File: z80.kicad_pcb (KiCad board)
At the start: 2 copper layers, 104.1 x 121.9 mm, 53 parts, among them P1 CONN_02X20, SW1 RESET, SW2 STEP, U1 Z80CPU, U2 74HC04, U3 74LS138, U4 LM555N, U5 74HC74, U6 LM555N, Y1 7.3728MHz

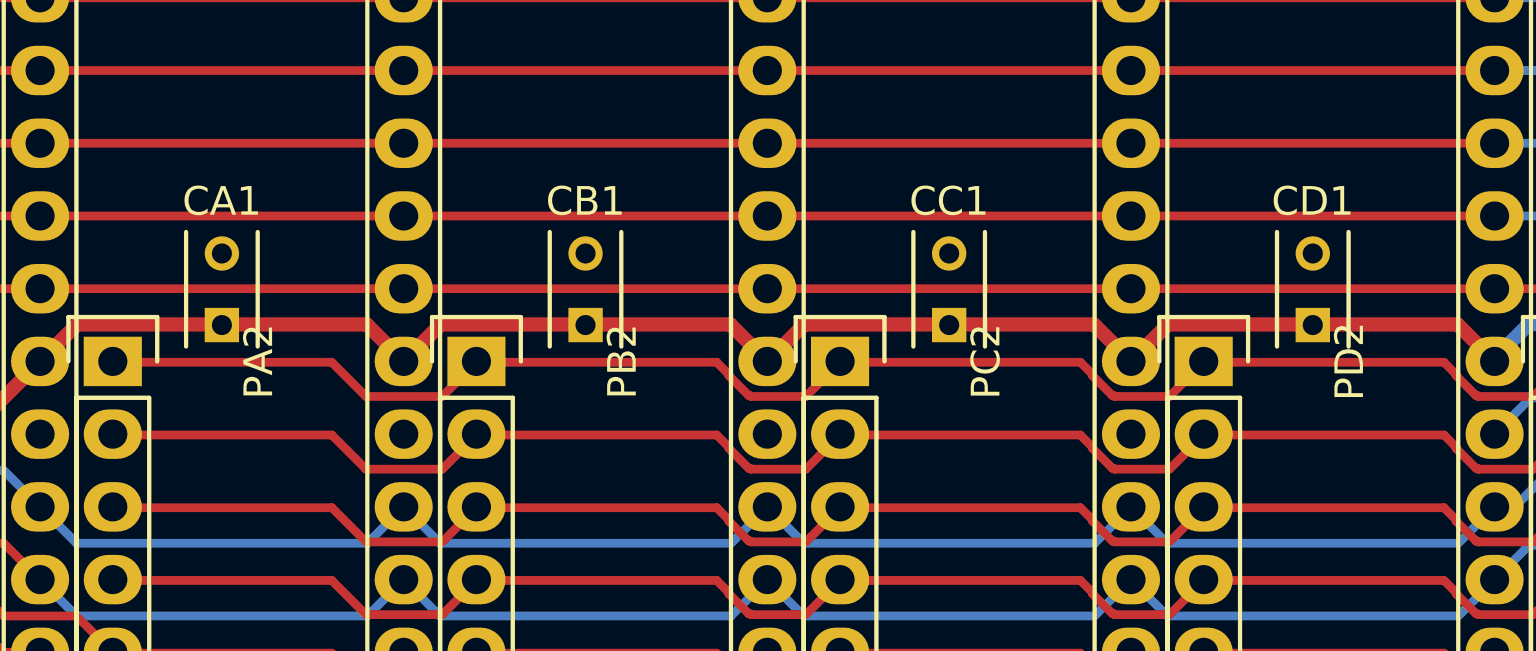
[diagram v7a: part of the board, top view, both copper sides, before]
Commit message: Flipped the decoupling caps around for neatness
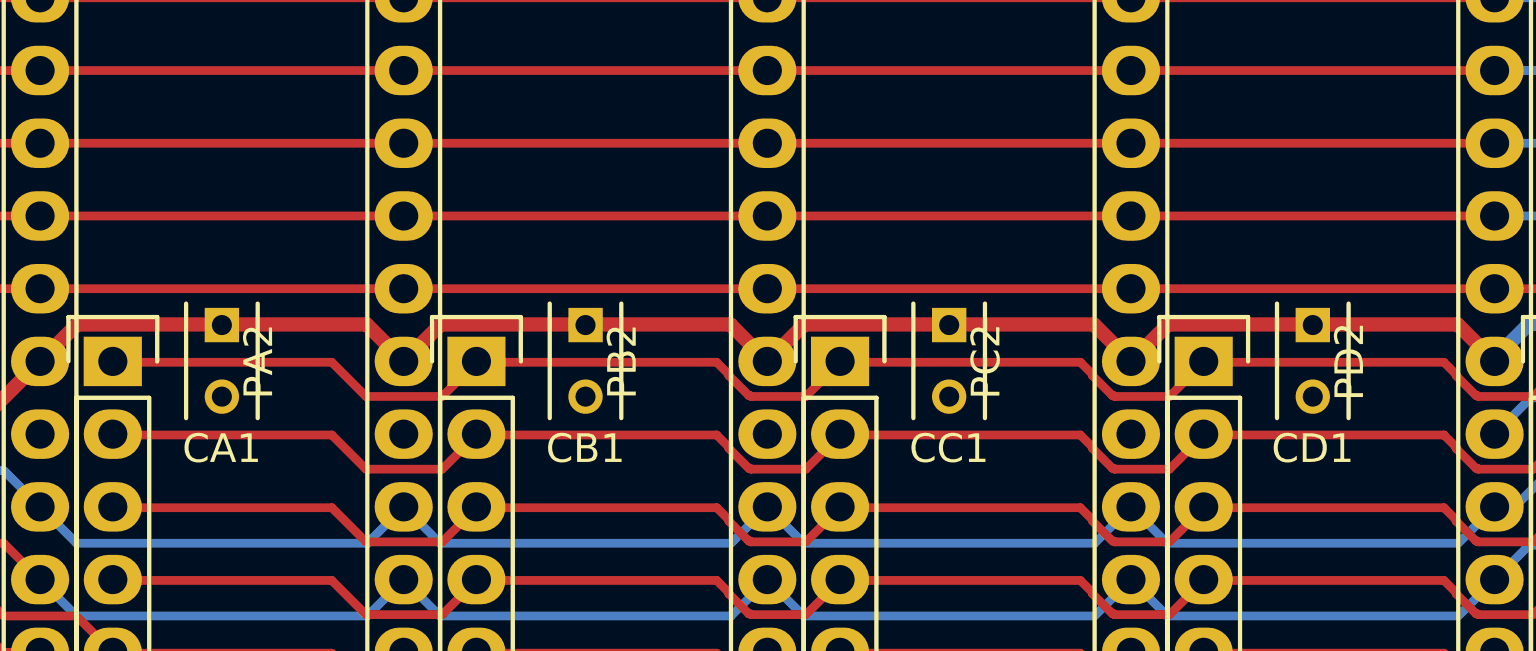
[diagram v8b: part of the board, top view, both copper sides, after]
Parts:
- turned CA1 to 270 degrees
- turned CB1 to 270 degrees
- turned CC1 to 270 degrees
- turned CD1 to 270 degrees
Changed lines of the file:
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@@
   )
   (module Capacitors_ThroughHole:C_Rect_L4_W2.5_P2.5 (layer Top)
-    (at 77.47 77.47 90)
-    (descr "Film Capacitor Length 4mm x Width 2.5mm, Pitch 2.5mm")
-    (tags Capacitor)
-    (fp_text reference CA1 (at 4.318 0 180) (layer F.SilkS)
-      (effects (font (size 1 1) (thickness 0.15)))
-    )
-    (fp_text value 100n (at 1.25 2.5 90) (layer F.Fab)
-      (effects (font (size 1 1) (thickness 0.15)))
-    )
-    (fp_line (start -1 -1.5) (end 3.5 -1.5) (layer F.CrtYd) (width 0.05))
-    (fp_line (start 3.5 -1.5) (end 3.5 1.5) (layer F.CrtYd) (width 0.05))
-    (fp_line (start 3.5 1.5) (end -1 1.5) (layer F.CrtYd) (width 0.05))
-    (fp_line (start -1 1.5) (end -1 -1.5) (layer F.CrtYd) (width 0.05))
-    (fp_line (start -0.75 -1.25) (end 3.25 -1.25) (layer F.SilkS) (width 0.15))
-    (fp_line (start -0.75 1.25) (end 3.25 1.25) (layer F.SilkS) (width 0.15))
-    (pad 1 thru_hole rect (at 0 0 90) (size 1.2 1.2) (drill 0.7) (layers *.Cu *.Mask F.SilkS)
-      (net 1 VCC))
-    (pad 2 thru_hole circle (at 2.5 0 90) (size 1.2 1.2) (drill 0.7) (layers *.Cu *.Mask F.SilkS)
-      (net 2 GND))
-  )
-  (module Capacitors_ThroughHole:C_Rect_L4_W2.5_P2.5 (layer Top)
-    (at 102.87 77.47 90)
-    (descr "Film Capacitor Length 4mm x Width 2.5mm, Pitch 2.5mm")
-    (tags Capacitor)
-    (fp_text reference CC1 (at 4.318 0 180) (layer F.SilkS)
-      (effects (font (size 1 1) (thickness 0.15)))
-    )
-    (fp_text value 100n (at 1.25 2.5 90) (layer F.Fab)
-      (effects (font (size 1 1) (thickness 0.15)))
-    )
-    (fp_line (start -1 -1.5) (end 3.5 -1.5) (layer F.CrtYd) (width 0.05))
-    (fp_line (start 3.5 -1.5) (end 3.5 1.5) (layer F.CrtYd) (width 0.05))
-    (fp_line (start 3.5 1.5) (end -1 1.5) (layer F.CrtYd) (width 0.05))
-    (fp_line (start -1 1.5) (end -1 -1.5) (layer F.CrtYd) (width 0.05))
-    (fp_line (start -0.75 -1.25) (end 3.25 -1.25) (layer F.SilkS) (width 0.15))
-    (fp_line (start -0.75 1.25) (end 3.25 1.25) (layer F.SilkS) (width 0.15))
-    (pad 1 thru_hole rect (at 0 0 90) (size 1.2 1.2) (drill 0.7) (layers *.Cu *.Mask F.SilkS)
-      (net 1 VCC))
-    (pad 2 thru_hole circle (at 2.5 0 90) (size 1.2 1.2) (drill 0.7) (layers *.Cu *.Mask F.SilkS)
+    (at 77.47 77.47 270)
+    (descr "Film Capacitor Length 4mm x Width 2.5mm, Pitch 2.5mm")
+    (tags Capacitor)
+    (fp_text reference CA1 (at 4.318 0 360) (layer F.SilkS)
+      (effects (font (size 1 1) (thickness 0.15)))
+    )
+    (fp_text value 100n (at 1.25 2.5 270) (layer F.Fab)
+      (effects (font (size 1 1) (thickness 0.15)))
+    )
+    (fp_line (start -1 -1.5) (end 3.5 -1.5) (layer F.CrtYd) (width 0.05))
+    (fp_line (start 3.5 -1.5) (end 3.5 1.5) (layer F.CrtYd) (width 0.05))
+    (fp_line (start 3.5 1.5) (end -1 1.5) (layer F.CrtYd) (width 0.05))
+    (fp_line (start -1 1.5) (end -1 -1.5) (layer F.CrtYd) (width 0.05))
+    (fp_line (start -0.75 -1.25) (end 3.25 -1.25) (layer F.SilkS) (width 0.15))
+    (fp_line (start -0.75 1.25) (end 3.25 1.25) (layer F.SilkS) (width 0.15))
+    (pad 1 thru_hole rect (at 0 0 270) (size 1.2 1.2) (drill 0.7) (layers *.Cu *.Mask F.SilkS)
+      (net 1 VCC))
+    (pad 2 thru_hole circle (at 2.5 0 270) (size 1.2 1.2) (drill 0.7) (layers *.Cu *.Mask F.SilkS)
+      (net 2 GND))
+  )
+  (module Capacitors_ThroughHole:C_Rect_L4_W2.5_P2.5 (layer Top)
+    (at 102.87 77.47 270)
+    (descr "Film Capacitor Length 4mm x Width 2.5mm, Pitch 2.5mm")
+    (tags Capacitor)
+    (fp_text reference CC1 (at 4.318 0 360) (layer F.SilkS)
+      (effects (font (size 1 1) (thickness 0.15)))
+    )
+    (fp_text value 100n (at 1.25 2.5 270) (layer F.Fab)
+      (effects (font (size 1 1) (thickness 0.15)))
+    )
+    (fp_line (start -1 -1.5) (end 3.5 -1.5) (layer F.CrtYd) (width 0.05))
+    (fp_line (start 3.5 -1.5) (end 3.5 1.5) (layer F.CrtYd) (width 0.05))
+    (fp_line (start 3.5 1.5) (end -1 1.5) (layer F.CrtYd) (width 0.05))
+    (fp_line (start -1 1.5) (end -1 -1.5) (layer F.CrtYd) (width 0.05))
+    (fp_line (start -0.75 -1.25) (end 3.25 -1.25) (layer F.SilkS) (width 0.15))
+    (fp_line (start -0.75 1.25) (end 3.25 1.25) (layer F.SilkS) (width 0.15))
+    (pad 1 thru_hole rect (at 0 0 270) (size 1.2 1.2) (drill 0.7) (layers *.Cu *.Mask F.SilkS)
+      (net 1 VCC))
+    (pad 2 thru_hole circle (at 2.5 0 270) (size 1.2 1.2) (drill 0.7) (layers *.Cu *.Mask F.SilkS)
       (net 2 GND))
   )
@@
   )
   (module Capacitors_ThroughHole:C_Rect_L4_W2.5_P2.5 (layer Top)
-    (at 90.17 77.47 90)
-    (descr "Film Capacitor Length 4mm x Width 2.5mm, Pitch 2.5mm")
-    (tags Capacitor)
-    (fp_text reference CB1 (at 4.318 0 180) (layer F.SilkS)
-      (effects (font (size 1 1) (thickness 0.15)))
-    )
-    (fp_text value 100n (at 1.25 2.5 90) (layer F.Fab)
-      (effects (font (size 1 1) (thickness 0.15)))
-    )
-    (fp_line (start -1 -1.5) (end 3.5 -1.5) (layer F.CrtYd) (width 0.05))
-    (fp_line (start 3.5 -1.5) (end 3.5 1.5) (layer F.CrtYd) (width 0.05))
-    (fp_line (start 3.5 1.5) (end -1 1.5) (layer F.CrtYd) (width 0.05))
-    (fp_line (start -1 1.5) (end -1 -1.5) (layer F.CrtYd) (width 0.05))
-    (fp_line (start -0.75 -1.25) (end 3.25 -1.25) (layer F.SilkS) (width 0.15))
-    (fp_line (start -0.75 1.25) (end 3.25 1.25) (layer F.SilkS) (width 0.15))
-    (pad 1 thru_hole rect (at 0 0 90) (size 1.2 1.2) (drill 0.7) (layers *.Cu *.Mask F.SilkS)
-      (net 1 VCC))
-    (pad 2 thru_hole circle (at 2.5 0 90) (size 1.2 1.2) (drill 0.7) (layers *.Cu *.Mask F.SilkS)
-      (net 2 GND))
-  )
-  (module Capacitors_ThroughHole:C_Rect_L4_W2.5_P2.5 (layer Top)
-    (at 115.57 77.47 90)
-    (descr "Film Capacitor Length 4mm x Width 2.5mm, Pitch 2.5mm")
-    (tags Capacitor)
-    (fp_text reference CD1 (at 4.318 0 180) (layer F.SilkS)
-      (effects (font (size 1 1) (thickness 0.15)))
-    )
-    (fp_text value 100n (at 1.25 2.5 90) (layer F.Fab)
-      (effects (font (size 1 1) (thickness 0.15)))
-    )
-    (fp_line (start -1 -1.5) (end 3.5 -1.5) (layer F.CrtYd) (width 0.05))
-    (fp_line (start 3.5 -1.5) (end 3.5 1.5) (layer F.CrtYd) (width 0.05))
-    (fp_line (start 3.5 1.5) (end -1 1.5) (layer F.CrtYd) (width 0.05))
-    (fp_line (start -1 1.5) (end -1 -1.5) (layer F.CrtYd) (width 0.05))
-    (fp_line (start -0.75 -1.25) (end 3.25 -1.25) (layer F.SilkS) (width 0.15))
-    (fp_line (start -0.75 1.25) (end 3.25 1.25) (layer F.SilkS) (width 0.15))
-    (pad 1 thru_hole rect (at 0 0 90) (size 1.2 1.2) (drill 0.7) (layers *.Cu *.Mask F.SilkS)
-      (net 1 VCC))
-    (pad 2 thru_hole circle (at 2.5 0 90) (size 1.2 1.2) (drill 0.7) (layers *.Cu *.Mask F.SilkS)
-      (net 2 GND))
-  )
+    (at 90.17 77.47 270)
+    (descr "Film Capacitor Length 4mm x Width 2.5mm, Pitch 2.5mm")
+    (tags Capacitor)
+    (fp_text reference CB1 (at 4.318 0 360) (layer F.SilkS)
+      (effects (font (size 1 1) (thickness 0.15)))
+    )
+    (fp_text value 100n (at 1.25 2.5 270) (layer F.Fab)
+      (effects (font (size 1 1) (thickness 0.15)))
+    )
+    (fp_line (start -1 -1.5) (end 3.5 -1.5) (layer F.CrtYd) (width 0.05))
+    (fp_line (start 3.5 -1.5) (end 3.5 1.5) (layer F.CrtYd) (width 0.05))
+    (fp_line (start 3.5 1.5) (end -1 1.5) (layer F.CrtYd) (width 0.05))
+    (fp_line (start -1 1.5) (end -1 -1.5) (layer F.CrtYd) (width 0.05))
+    (fp_line (start -0.75 -1.25) (end 3.25 -1.25) (layer F.SilkS) (width 0.15))
+    (fp_line (start -0.75 1.25) (end 3.25 1.25) (layer F.SilkS) (width 0.15))
+    (pad 1 thru_hole rect (at 0 0 270) (size 1.2 1.2) (drill 0.7) (layers *.Cu *.Mask F.SilkS)
+      (net 1 VCC))
+    (pad 2 thru_hole circle (at 2.5 0 270) (size 1.2 1.2) (drill 0.7) (layers *.Cu *.Mask F.SilkS)
+      (net 2 GND))
+  )
+  (module Capacitors_ThroughHole:C_Rect_L4_W2.5_P2.5 (layer Top)
+    (at 115.57 77.47 270)
+    (descr "Film Capacitor Length 4mm x Width 2.5mm, Pitch 2.5mm")
+    (tags Capacitor)
+    (fp_text reference CD1 (at 4.318 0 360) (layer F.SilkS)
+      (effects (font (size 1 1) (thickness 0.15)))
+    )
+    (fp_text value 100n (at 1.25 2.5 270) (layer F.Fab)
+      (effects (font (size 1 1) (thickness 0.15)))
+    )
+    (fp_line (start -1 -1.5) (end 3.5 -1.5) (layer F.CrtYd) (width 0.05))
+    (fp_line (start 3.5 -1.5) (end 3.5 1.5) (layer F.CrtYd) (width 0.05))
+    (fp_line (start 3.5 1.5) (end -1 1.5) (layer F.CrtYd) (width 0.05))
+    (fp_line (start -1 1.5) (end -1 -1.5) (layer F.CrtYd) (width 0.05))
+    (fp_line (start -0.75 -1.25) (end 3.25 -1.25) (layer F.SilkS) (width 0.15))
+    (fp_line (start -0.75 1.25) (end 3.25 1.25) (layer F.SilkS) (width 0.15))
+    (pad 1 thru_hole rect (at 0 0 270) (size 1.2 1.2) (drill 0.7) (layers *.Cu *.Mask F.SilkS)
+      (net 1 VCC))
+    (pad 2 thru_hole circle (at 2.5 0 270) (size 1.2 1.2) (drill 0.7) (layers *.Cu *.Mask F.SilkS)
+      (net 2 GND))
+  )
